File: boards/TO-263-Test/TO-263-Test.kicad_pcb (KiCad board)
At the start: 2 copper layers, 43.2 x 26.7 mm, 3 parts, among them J1 Conn_01x02, J2 Conn_01x02

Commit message: Adding changes to the TO-263 Test board
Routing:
- net Net-(J2-Pad1): track 16.4 -> 18.9 mm
- net Net-(J1-Pad1): track 17.1 -> 19.6 mm
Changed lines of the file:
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@@
   (general
     (links 4)
-    (no_connects 0)
-    (area 119.304999 91.364999 162.635001 118.185001)
+    (no_connects 2)
+    (area 118.442381 90.01 162.635001 118.185001)
     (thickness 1.6)
     (drawings 10)
-    (tracks 6)
+    (tracks 8)
     (zones 0)
     (modules 3)
@@
   (gr_arc (start 121.92 115.57) (end 121.92 118.11) (angle 90) (layer Edge.Cuts) (width 0.15))
   (gr_arc (start 121.92 93.98) (end 119.38 93.98) (angle 90) (layer Edge.Cuts) (width 0.15))
+  (segment (start 121.92 96.52) (end 124.46 96.52) (width 0.25) (layer F.Cu) (net 1))
   (segment (start 124.46 96.52) (end 133.6635 96.52) (width 0.25) (layer F.Cu) (net 1))
   (segment (start 133.6635 96.52) (end 138.3411 101.1976) (width 0.25) (layer F.Cu) (net 1))
   (segment (start 138.3411 101.1976) (end 138.3411 102.4636) (width 0.25) (layer F.Cu) (net 1))
+  (segment (start 121.92 111.76) (end 124.46 111.76) (width 0.25) (layer F.Cu) (net 2))
   (segment (start 124.46 111.76) (end 135.3907 111.76) (width 0.25) (layer F.Cu) (net 2))
   (segment (start 135.3907 111.76) (end 138.3411 108.8096) (width 0.25) (layer F.Cu) (net 2))

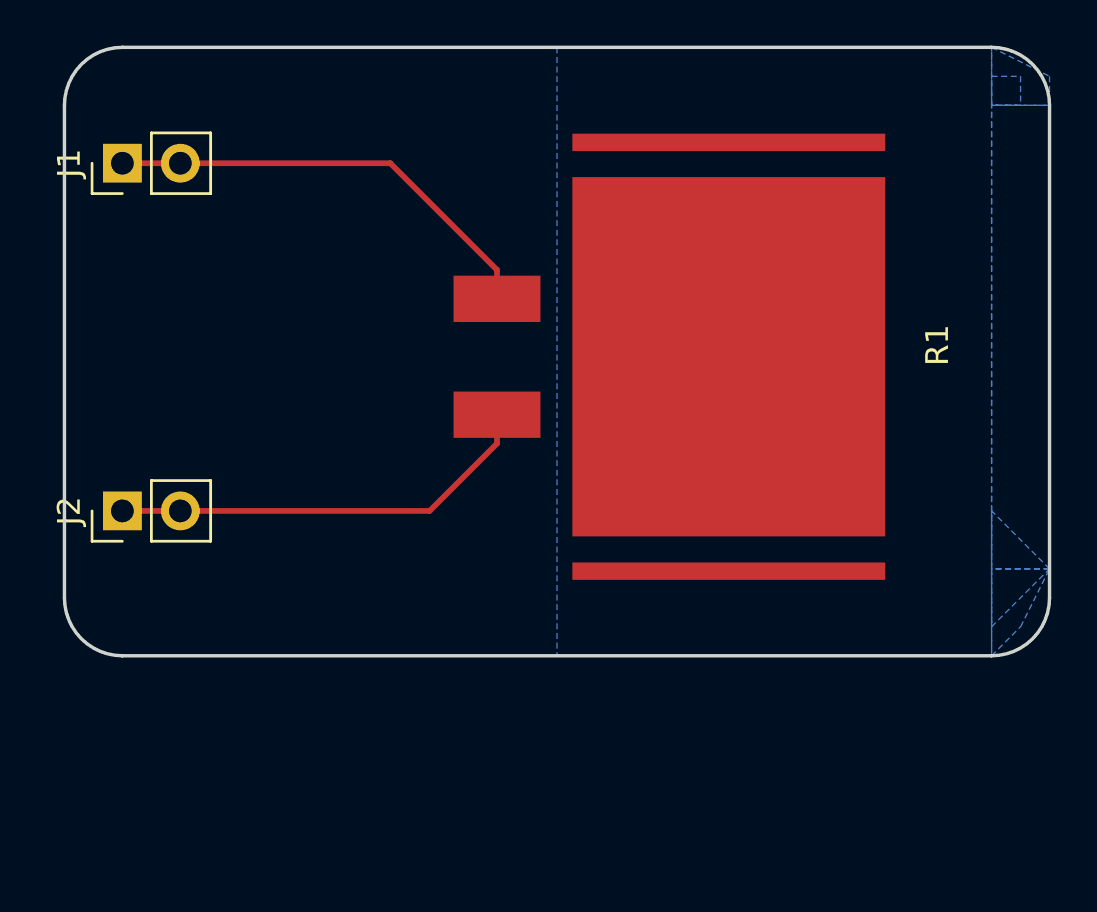
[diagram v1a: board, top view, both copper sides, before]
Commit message: Adding TSAL 1.0 with gerber and drill files in PostScript format
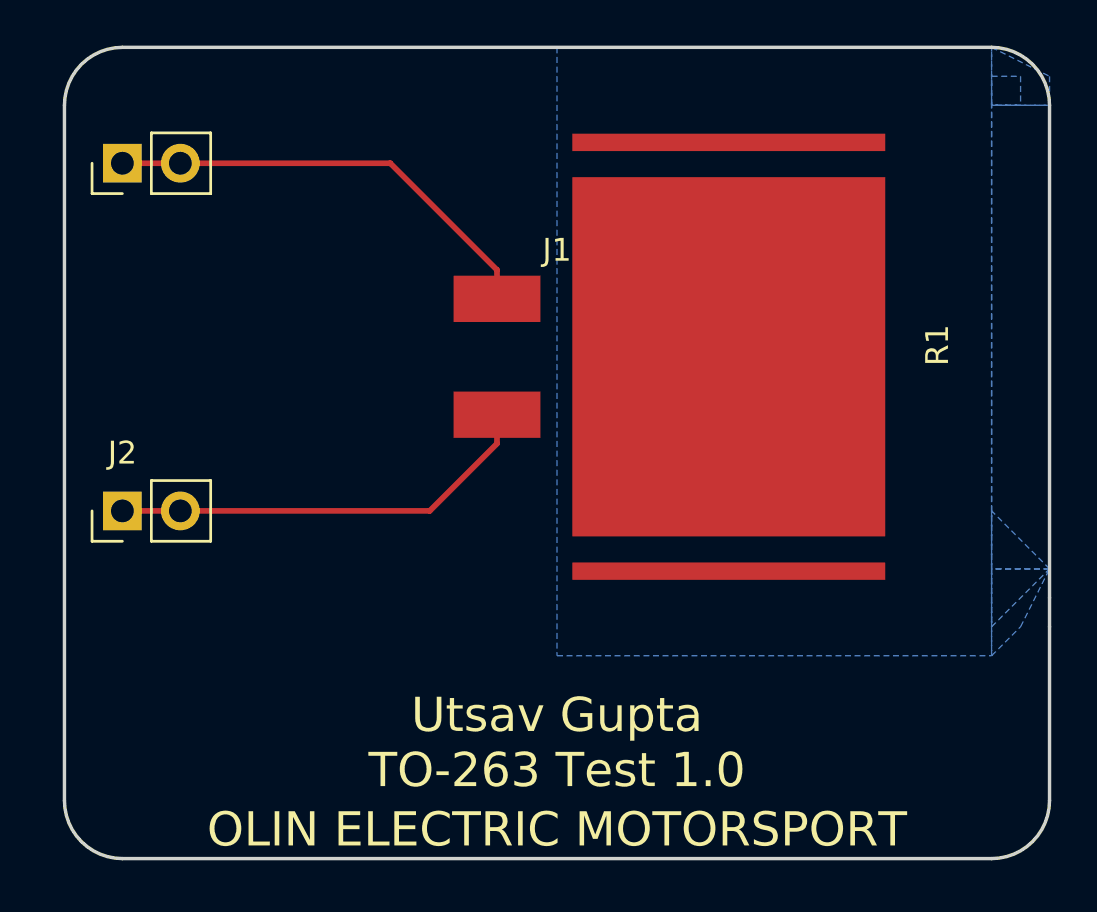
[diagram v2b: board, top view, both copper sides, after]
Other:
- board size 43.2 x 26.7 mm -> 43.2 x 35.6 mm
- board text added: "OLIN ELECTRIC MOTORSPORT"
- board text added: "Utsav Gupta TO-263 Test 1.0"
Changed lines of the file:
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@@
   (general
     (links 4)
-    (no_connects 2)
-    (area 118.442381 90.01 162.635001 118.185001)
+    (no_connects 0)
+    (area 119.304999 91.364999 162.635001 127.08)
     (thickness 1.6)
-    (drawings 10)
+    (drawings 12)
     (tracks 8)
     (zones 0)
@@
     (visible_elements FFFFFF7F)
     (pcbplotparams
-      (layerselection 0x00030_80000001)
+      (layerselection 0x010f0_80000001)
       (usegerberextensions false)
       (excludeedgelayer true)
@@
       (outputformat 1)
       (mirror false)
-      (drillshape 1)
+      (drillshape 0)
       (scaleselection 1)
-      (outputdirectory ""))
+      (outputdirectory /home/utsav22g/Desktop/Formula/OEM/MK_III-Boards/boards/TO-263-Test/Gerbers/))
   )
   (net 0 "")
@@
     (descr "Through hole straight pin header, 1x02, 2.54mm pitch, single row")
     (tags "Through hole pin header THT 1x02 2.54mm single row")
-    (fp_text reference J1 (at 0 -2.33 90) (layer F.SilkS)
-      (effects (font (size 1 1) (thickness 0.15)))
-    )
-    (fp_text value Conn_01x02 (at 2.54 1.27 360) (layer F.Fab)
+    (fp_text reference J1 (at -3.81 19.05 180) (layer F.SilkS)
+      (effects (font (size 1 1) (thickness 0.15)))
+    )
+    (fp_text value Conn_01x02 (at 2.54 2.54 360) (layer F.Fab)
       (effects (font (size 1 1) (thickness 0.15)))
     )
@@
     (descr "Through hole straight pin header, 1x02, 2.54mm pitch, single row")
     (tags "Through hole pin header THT 1x02 2.54mm single row")
-    (fp_text reference J2 (at 0 -2.33 90) (layer F.SilkS)
-      (effects (font (size 1 1) (thickness 0.15)))
-    )
-    (fp_text value Conn_01x02 (at -2.54 1.27 360) (layer F.Fab)
+    (fp_text reference J2 (at 2.54 0 180) (layer F.SilkS)
+      (effects (font (size 1 1) (thickness 0.15)))
+    )
+    (fp_text value Conn_01x02 (at -2.54 2.54 360) (layer F.Fab)
       (effects (font (size 1 1) (thickness 0.15)))
     )
@@
     )
   )
-  (dimension 15.24 (width 0.3) (layer F.SilkS)
-    (gr_text "15.240 mm" (at 133.35 91.36) (layer F.SilkS)
-      (effects (font (size 1.5 1.5) (thickness 0.3)))
-    )
-    (feature1 (pts (xy 140.97 96.52) (xy 140.97 90.01)))
-    (feature2 (pts (xy 125.73 96.52) (xy 125.73 90.01)))
-    (crossbar (pts (xy 125.73 92.71) (xy 140.97 92.71)))
-    (arrow1a (pts (xy 140.97 92.71) (xy 139.843496 93.296421)))
-    (arrow1b (pts (xy 140.97 92.71) (xy 139.843496 92.123579)))
-    (arrow2a (pts (xy 125.73 92.71) (xy 126.856504 93.296421)))
-    (arrow2b (pts (xy 125.73 92.71) (xy 126.856504 92.123579)))
-  )
-  (dimension 12.7 (width 0.3) (layer F.SilkS)
-    (gr_text "12.700 mm" (at 128.35 104.14 270) (layer F.SilkS)
-      (effects (font (size 1.5 1.5) (thickness 0.3)))
-    )
-    (feature1 (pts (xy 121.92 110.49) (xy 129.7 110.49)))
-    (feature2 (pts (xy 121.92 97.79) (xy 129.7 97.79)))
-    (crossbar (pts (xy 127 97.79) (xy 127 110.49)))
-    (arrow1a (pts (xy 127 110.49) (xy 126.413579 109.363496)))
-    (arrow1b (pts (xy 127 110.49) (xy 127.586421 109.363496)))
-    (arrow2a (pts (xy 127 97.79) (xy 126.413579 98.916504)))
-    (arrow2b (pts (xy 127 97.79) (xy 127.586421 98.916504)))
-  )
-  (gr_line (start 121.92 118.11) (end 160.02 118.11) (angle 90) (layer Edge.Cuts) (width 0.15))
-  (gr_line (start 119.38 93.98) (end 119.38 115.57) (angle 90) (layer Edge.Cuts) (width 0.15))
+  (gr_line (start 121.92 127) (end 160.02 127) (layer Edge.Cuts) (width 0.15))
+  (gr_line (start 119.38 93.98) (end 119.38 124.46) (layer Edge.Cuts) (width 0.15))
+  (gr_arc (start 121.92 124.46) (end 121.92 127) (angle 90) (layer Edge.Cuts) (width 0.15))
+  (gr_line (start 162.56 116.84) (end 162.56 115.57) (layer Edge.Cuts) (width 0.15))
+  (gr_line (start 162.56 124.46) (end 162.56 116.84) (layer Edge.Cuts) (width 0.15))
+  (gr_arc (start 160.02 124.46) (end 162.56 124.46) (angle 90) (layer Edge.Cuts) (width 0.15))
+  (gr_text "OLIN ELECTRIC MOTORSPORT\n" (at 140.97 125.73) (layer F.SilkS)
+    (effects (font (size 1.5 1.5) (thickness 0.3)))
+  )
+  (gr_text "Utsav Gupta\nTO-263 Test 1.0" (at 140.97 121.92) (layer F.SilkS)
+    (effects (font (size 1.5 1.5) (thickness 0.3)))
+  )
   (gr_line (start 162.56 93.98) (end 162.56 115.57) (angle 90) (layer Edge.Cuts) (width 0.15))
   (gr_line (start 121.92 91.44) (end 160.02 91.44) (angle 90) (layer Edge.Cuts) (width 0.15))
-  (gr_arc (start 160.02 115.57) (end 162.56 115.57) (angle 90) (layer Edge.Cuts) (width 0.15))
   (gr_arc (start 160.02 93.98) (end 160.02 91.44) (angle 90) (layer Edge.Cuts) (width 0.15))
-  (gr_arc (start 121.92 115.57) (end 121.92 118.11) (angle 90) (layer Edge.Cuts) (width 0.15))
   (gr_arc (start 121.92 93.98) (end 119.38 93.98) (angle 90) (layer Edge.Cuts) (width 0.15))
   (segment (start 121.92 96.52) (end 124.46 96.52) (width 0.25) (layer F.Cu) (net 1))
@@
     (polygon
       (pts
+        (xy 160.02 93.98) (xy 162.56 93.98) (xy 162.56 114.3) (xy 160.02 114.3)
+      )
+    )
+  )
+  (zone (net 0) (net_name "") (layer B.Cu) (hatch edge 0.508)
+    (connect_pads (clearance 0.508))
+    (min_thickness 0.254)
+    (fill yes (arc_segments 16) (thermal_gap 0.508) (thermal_bridge_width 0.508))
+    (polygon
+      (pts
+        (xy 160.02 92.71) (xy 161.29 92.71) (xy 161.29 93.98) (xy 160.02 93.98)
+      )
+    )
+  )
+  (zone (net 0) (net_name "") (layer B.Cu) (hatch edge 0.508)
+    (connect_pads (clearance 0.508))
+    (min_thickness 0.254)
+    (fill yes (arc_segments 16) (thermal_gap 0.508) (thermal_bridge_width 0.508))
+    (polygon
+      (pts
+        (xy 160.02 116.84) (xy 162.56 114.3) (xy 160.02 114.3)
+      )
+    )
+  )
+  (zone (net 0) (net_name "") (layer B.Cu) (hatch edge 0.508)
+    (connect_pads (clearance 0.508))
+    (min_thickness 0.254)
+    (fill yes (arc_segments 16) (thermal_gap 0.508) (thermal_bridge_width 0.508))
+    (polygon
+      (pts
+        (xy 160.02 118.11) (xy 161.29 116.84) (xy 162.56 114.3) (xy 160.02 111.76)
+      )
+    )
+  )
+  (zone (net 0) (net_name "") (layer B.Cu) (hatch edge 0.508)
+    (connect_pads (clearance 0.508))
+    (min_thickness 0.254)
+    (fill yes (arc_segments 16) (thermal_gap 0.508) (thermal_bridge_width 0.508))
+    (polygon
+      (pts
+        (xy 160.02 93.98) (xy 160.02 91.44) (xy 162.56 92.71) (xy 162.56 93.98)
+      )
+    )
+  )
+  (zone (net 0) (net_name "") (layer B.Cu) (hatch edge 0.508)
+    (connect_pads (clearance 0.508))
+    (min_thickness 0.254)
+    (fill yes (arc_segments 16) (thermal_gap 0.508) (thermal_bridge_width 0.508))
+    (polygon
+      (pts
         (xy 140.97 91.44) (xy 140.97 118.11) (xy 160.02 118.11) (xy 160.02 91.44)
       )
     )
-  )
-  (zone (net 0) (net_name "") (layer B.Cu) (hatch edge 0.508)
-    (connect_pads (clearance 0.508))
-    (min_thickness 0.254)
-    (fill yes (arc_segments 16) (thermal_gap 0.508) (thermal_bridge_width 0.508))
-    (polygon
-      (pts
-        (xy 160.02 93.98) (xy 162.56 93.98) (xy 162.56 114.3) (xy 160.02 114.3)
-      )
-    )
-  )
-  (zone (net 0) (net_name "") (layer B.Cu) (hatch edge 0.508)
-    (connect_pads (clearance 0.508))
-    (min_thickness 0.254)
-    (fill yes (arc_segments 16) (thermal_gap 0.508) (thermal_bridge_width 0.508))
-    (polygon
-      (pts
-        (xy 160.02 92.71) (xy 161.29 92.71) (xy 161.29 93.98) (xy 160.02 93.98)
-      )
-    )
-  )
-  (zone (net 0) (net_name "") (layer B.Cu) (hatch edge 0.508)
-    (connect_pads (clearance 0.508))
-    (min_thickness 0.254)
-    (fill yes (arc_segments 16) (thermal_gap 0.508) (thermal_bridge_width 0.508))
-    (polygon
-      (pts
-        (xy 160.02 116.84) (xy 162.56 114.3) (xy 160.02 114.3)
-      )
-    )
-  )
-  (zone (net 0) (net_name "") (layer B.Cu) (hatch edge 0.508)
-    (connect_pads (clearance 0.508))
-    (min_thickness 0.254)
-    (fill yes (arc_segments 16) (thermal_gap 0.508) (thermal_bridge_width 0.508))
-    (polygon
-      (pts
-        (xy 160.02 118.11) (xy 161.29 116.84) (xy 162.56 114.3) (xy 160.02 111.76)
-      )
-    )
-  )
-  (zone (net 0) (net_name "") (layer B.Cu) (hatch edge 0.508)
-    (connect_pads (clearance 0.508))
-    (min_thickness 0.254)
-    (fill yes (arc_segments 16) (thermal_gap 0.508) (thermal_bridge_width 0.508))
-    (polygon
-      (pts
-        (xy 160.02 93.98) (xy 160.02 91.44) (xy 162.56 92.71) (xy 162.56 93.98)
-      )
-    )
